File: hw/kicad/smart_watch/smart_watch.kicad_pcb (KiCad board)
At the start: 2 copper layers, 45 parts, among them J1 BATTERTY, J2 1051330001, J3 GC9A01, J4 JST_PH6, SW1 SW_Push, SW2 SW_Push, SW4 SW_Push, U1 STM32L476RGTx, U2 nPM1300-QEAA, U3 SHT41, U4 LIS2MDL, U5 CH340E

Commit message: start pcb
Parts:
- added R4: 10k, Resistor_SMD:R_0603_1608Metric, F.Cu at (92.7, 88.5)
- added SW3: SW_Push, smart_watch:TL6340, F.Cu at (110.5, 89.5)
- SW1, SW2, SW4: footprint Button_Switch_SMD:SW_SPST_TL3305A -> smart_watch:TL6340
- moved C50 110.0 mm to (214.7, 150.0)
- moved C51 110.0 mm to (214.7, 152.5)
- moved U3 97.2 mm to (187.8, 47.1)
- moved C30 89.0 mm to (189.5, 49.0)
- moved U2 87.0 mm to (62.0, 98.0)
- moved D1 81.2 mm to (202.6, 141.2)
- moved R30 79.1 mm to (185.5, 45.0), turned to -90 degrees
- moved R31 78.1 mm to (185.5, 49.0), turned to 90 degrees
- moved L20 76.2 mm to (46.5, 89.7), turned to -90 degrees
- moved L21 73.0 mm to (49.5, 99.3), turned to -90 degrees
- moved C25 70.7 mm to (48.0, 89.7), turned to -90 degrees
- moved C26 70.5 mm to (48.0, 99.3), turned to -90 degrees
- moved C27 64.0 mm to (55.0, 108.3), turned to -90 degrees
- moved R20 59.9 mm to (68.5, 107.7), turned to 90 degrees
- moved R21 57.8 mm to (70.0, 107.7), turned to 90 degrees
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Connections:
- SW1 pad 2: /BTN_2 -> /BTN_1
- SW2 pad 2: /BTN_3 -> /BTN_2
- SW4 pad 2: /BTN_1 -> /BTN_4
- U1 pad 10: /BTN_3 -> unconnected-(U1-PC2-Pad10)
- U1 pad 26: unconnected-(U1-PB0-Pad26) -> /BTN_2
- U1 pad 40: unconnected-(U1-PC9-Pad40) -> /BTN_3
- U1 pad 53: unconnected-(U1-PC12-Pad53) -> /BTN_4
- U1 pad 9: /BTN_2 -> unconnected-(U1-PC1-Pad9)
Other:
- rule pad_to_mask_clearance: 0 -> 0.0508

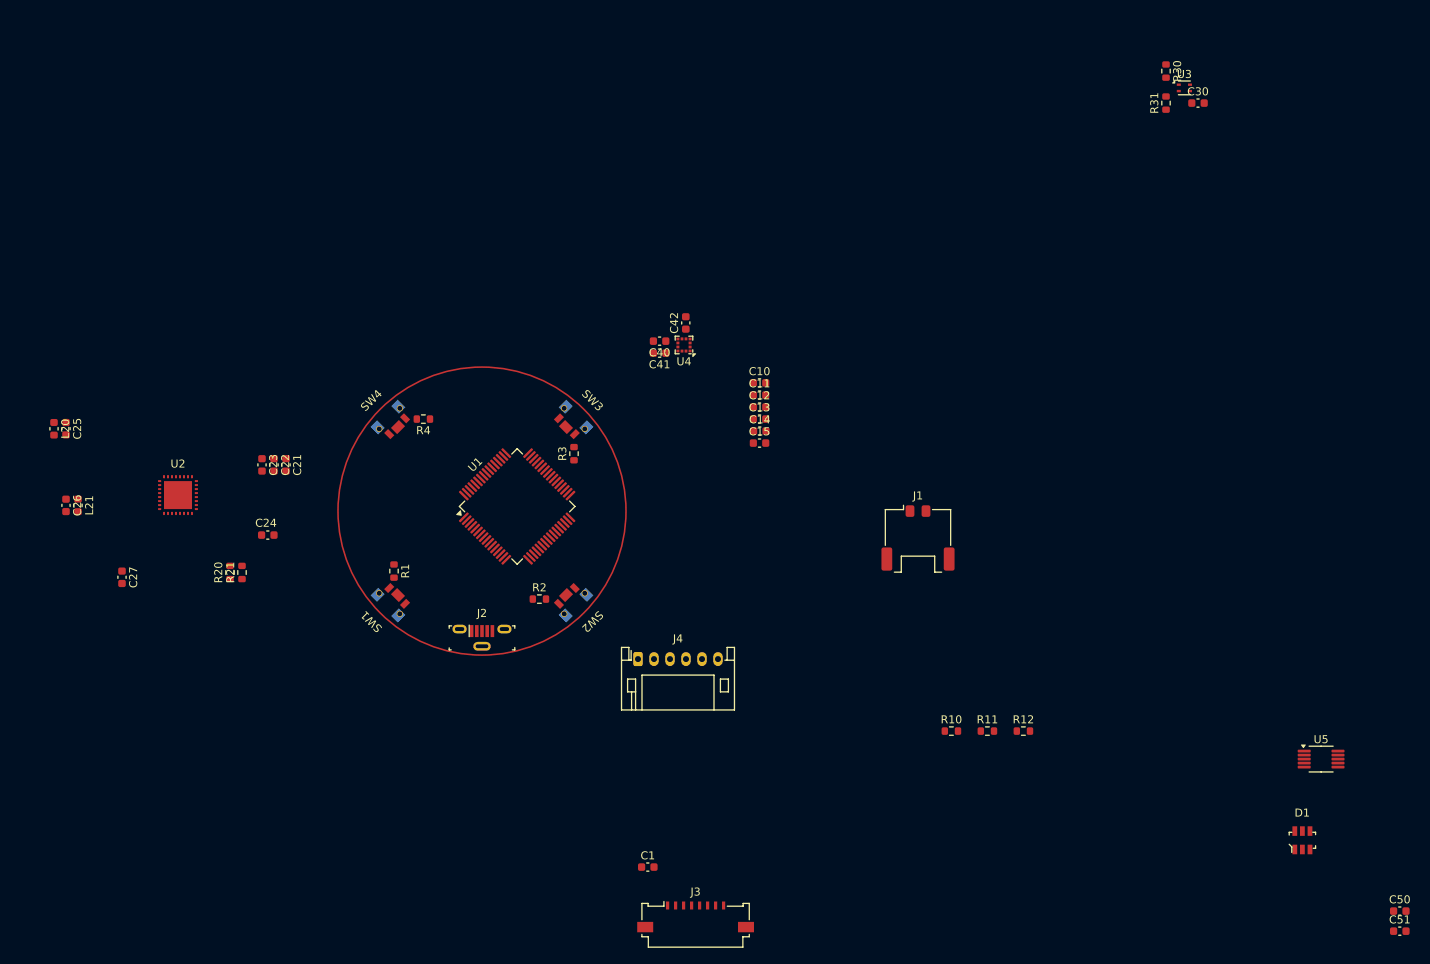
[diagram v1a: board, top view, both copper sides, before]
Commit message: added rtc chip to board
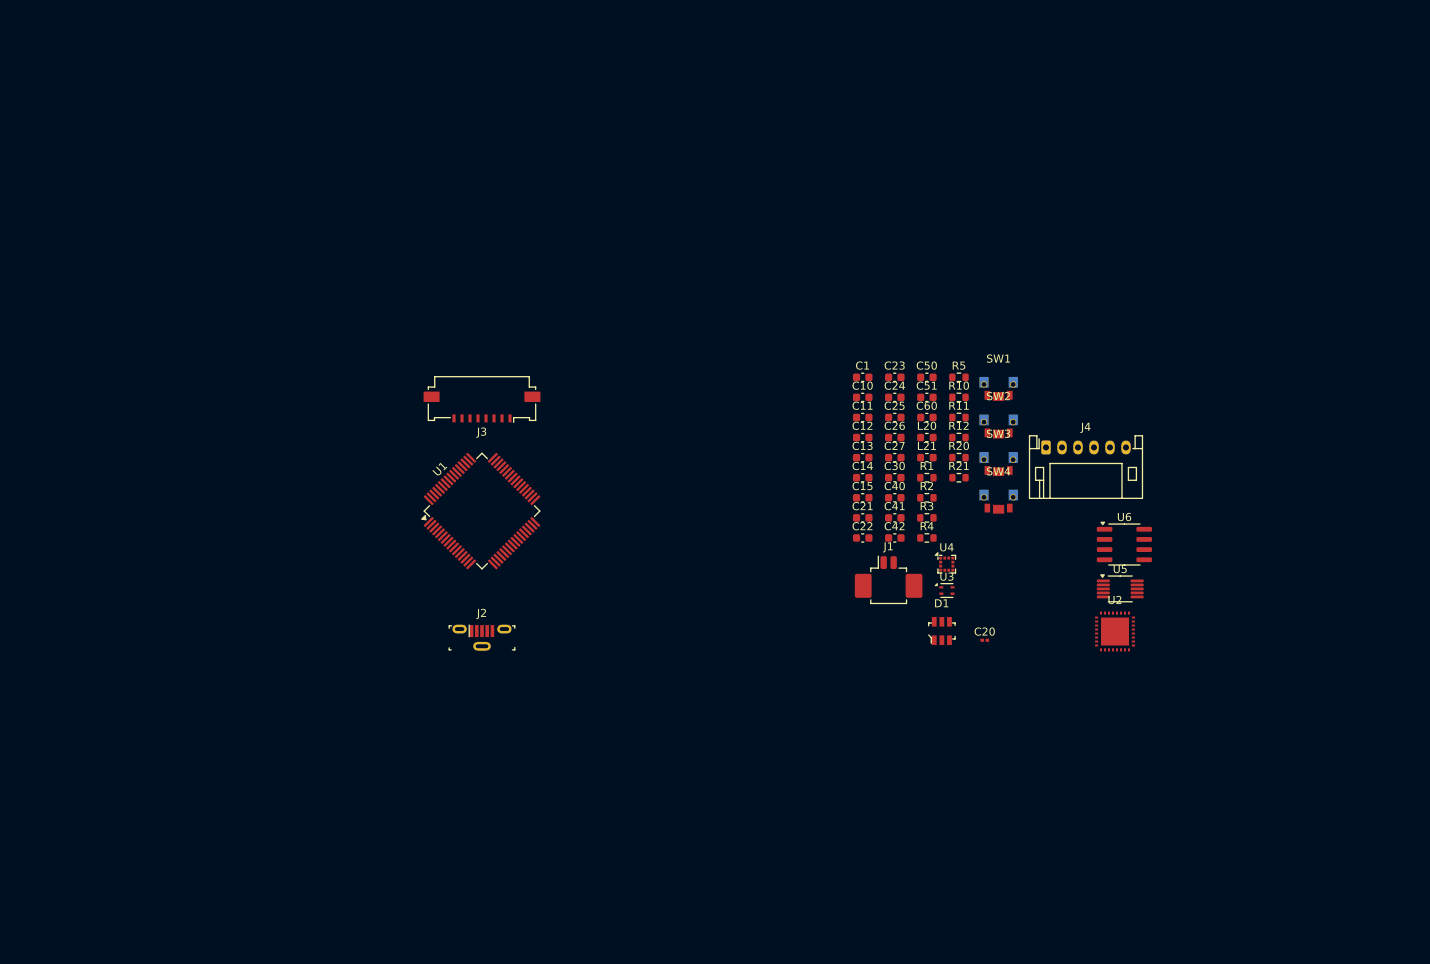
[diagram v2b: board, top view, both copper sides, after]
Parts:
- removed R30, R31: 10k, Resistor_SMD:R_0603_1608Metric
- added C20: 1u, Capacitor_SMD:C_0201_0603Metric, F.Cu at (162.8, 116.2)
- added C60: 100n, Capacitor_SMD:C_0603_1608Metric, F.Cu at (155.6, 88.3)
- added R5: 2.2k, Resistor_SMD:R_0603_1608Metric, F.Cu at (159.6, 83.3)
- added U6: DS3231MZ, Package_SO:SOIC-8_3.9x4.9mm_P1.27mm, F.Cu at (180.3, 104.2)
- C24, L21: value 220n -> 2.2u
- J1: footprint Connector_Molex:Molex_Pico-Lock_205338-0002_1x02-1MP_P2.00mm_Horizontal -> Connector_Molex:Molex_PicoBlade_53261-0271_1x02-1MP_P1.25mm_Horizontal
- L20: value 200n -> 2.2u
- moved U2 118.4 mm to (179.1, 115.1)
- moved L20 109.1 mm to (155.6, 90.8), turned to 0 degrees
- moved L21 106.3 mm to (155.6, 93.3), turned to 0 degrees
- moved C26 103.9 mm to (151.6, 90.8), turned to 0 degrees
- moved C25 103.6 mm to (151.6, 88.3), turned to 0 degrees
- moved C27 97.8 mm to (151.6, 93.3), turned to 0 degrees
- moved R20 92.2 mm to (159.6, 93.3), turned to 0 degrees
- moved R21 90.4 mm to (159.6, 95.8), turned to 0 degrees
- moved C50 89.1 mm to (155.6, 83.3)
- moved C51 89.1 mm to (155.6, 85.8)
- moved C24 80.2 mm to (151.6, 85.8)
- moved C23 79.9 mm to (151.6, 83.3), turned to 0 degrees
- moved SW1 79.1 mm to (164.6, 85.7), turned to 0 degrees
- moved SW4 75.8 mm to (164.6, 99.8), turned to 0 degrees
- moved C22 74.2 mm to (147.6, 103.4), turned to 0 degrees
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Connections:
- R11 pad 1: GND -> +3.3V
- R12 pad 2: GND -> +3.3V
- U1 pad 52: unconnected-(U1-PC11-Pad52) -> /RTC_INT

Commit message: pcb design part 1
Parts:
- C20: footprint Capacitor_SMD:C_0201_0603Metric -> Capacitor_SMD:C_0603_1608Metric
- J3: footprint Connector_FFC-FPC:Molex_200528-0080_1x08-1MP_P1.00mm_Horizontal -> Connector_FFC-FPC:Hirose_FH12-15S-0.5SH_1x15-1MP_P0.50mm_Horizontal; moved to B.Cu
- J4: value JST_PH6 -> JST_ZH6; footprint Connector_JST:JST_PH_S6B-PH-K_1x06_P2.00mm_Horizontal -> Connector_JST:JST_ZH_S6B-ZR-SM4A-TF_1x06-1MP_P1.50mm_Horizontal; moved to B.Cu
- moved U2 85.6 mm to (95.2, 98.0), turned to 180 degrees
- moved U6 82.6 mm to (100.0, 84.9), turned to 180 degrees
- moved SW1 80.3 mm to (88.5, 111.5), turned to 135 degrees
- moved SW4 76.9 mm to (88.5, 88.5), turned to 45 degrees
- moved U5 76.3 mm to (103.5, 111.2), turned to 90 degrees
- moved C20 72.9 mm to (91.8, 100.0), turned to -90 degrees
- moved R1 68.4 mm to (88.5, 108.9), turned to -90 degrees
- moved R20 66.4 mm to (93.2, 93.7), turned to -90 degrees
- moved R4 66.2 mm to (91.2, 88.2), turned to 180 degrees
- moved J1 66.1 mm to (85.3, 100.0), turned to -90 degrees
- moved R21 64.9 mm to (94.8, 93.7), turned to -90 degrees
- moved U4 63.1 mm to (97.5, 89.2)
- moved C24 60.6 mm to (91.8, 95.5), turned to 90 degrees
- moved C23 60.4 mm to (94.2, 102.3), turned to 90 degrees
- moved R11 59.8 mm to (101.0, 100.2), turned to -90 degrees
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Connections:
- D1 pad 4: Net-(U5-UD-) -> Net-(U5-UD+)
- D1 pad 6: Net-(U5-UD+) -> Net-(U5-UD-)
- J2 pad 2: Net-(D1-Pad3) -> Net-(D1-Pad1)
- J2 pad 3: Net-(D1-Pad1) -> Net-(D1-Pad3)
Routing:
- net +3.3V: track 0.00 -> 14.8 mm
- net +1.8V: track 0.00 -> 8.07 mm
- net Net-(J1-Pin_1): track 0.00 -> 7.80 mm
- net /VSYS: track 0.00 -> 4.24 mm
- net /I2C_SCL: track 0.00 -> 3.65 mm
- net Net-(U5-UD+): track 0.00 -> 2.89 mm
- net /I2C_SDA: track 0.00 -> 2.39 mm
- net Net-(U1-BOOT0): track 0.00 -> 2.32 mm
- net Net-(D1-Pad3): track 0.00 -> 2.31 mm
- net Net-(D1-Pad1): track 0.00 -> 2.21 mm
- net /RTC_INT: track 0.00 -> 1.94 mm
- net Net-(U2-VSET2): track 0.00 -> 1.91 mm
- net Net-(U2-VSET1): track 0.00 -> 1.89 mm
- net /VBUS: track 0.00 -> 1.59 mm
- net Net-(U4-C1): track 0.00 -> 1.25 mm
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
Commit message: pcb design part 2
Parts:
- added C16: 100n, Capacitor_SMD:C_0603_1608Metric, F.Cu at (101.9, 104.8)
- J4: moved to F.Cu
- moved J4 56.5 mm to (100.0, 87.6), turned to 180 degrees
- moved U4 22.2 mm to (106.6, 109.5)
- moved C42 22.1 mm to (106.1, 112.3)
- moved C40 22.1 mm to (109.4, 110.2)
- moved C41 22.1 mm to (109.4, 108.7)
- moved C15 20.8 mm to (105.1, 106.5), turned to 0 degrees
- moved J3 15.2 mm to (131.7, 85.5), turned to 0 degrees
- moved C12 14.6 mm to (115.4, 95.3)
- moved C30 14.6 mm to (91.9, 97.5)
- moved U3 14.5 mm to (94.7, 97.8)
- moved C60 10.7 mm to (98.8, 95.7)
- moved U6 10.7 mm to (94.3, 94.0)
- moved R5 10.6 mm to (98.8, 92.7), turned to 90 degrees
- moved C22 8.13 mm to (89.3, 105.7)
- moved C20 8.05 mm to (90.3, 108.0)
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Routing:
- net GND: track 0.00 -> 55.2 mm, vias 0 -> 28
- net /I2C_SDA: track 2.39 -> 37.2 mm, vias 0 -> 4
- net /BTN_1: track 0.00 -> 33.9 mm, vias 0 -> 2
- net +3.3V: track 14.8 -> 45.8 mm, vias 0 -> 13
- net /I2C_SCL: track 3.65 -> 33.3 mm, vias 0 -> 4
- net +1.8V: track 8.07 -> 33.5 mm, vias 0 -> 4
- net /BTN_2: track 0.00 -> 20.8 mm, vias 0 -> 2
- net /VBUS: track 1.59 -> 19.4 mm
- net /BTN_4: track 0.00 -> 17.2 mm, vias 0 -> 2
- net /VSYS: track 4.24 -> 19.4 mm, vias 0 -> 3
- net /RTC_INT: track 1.94 -> 11.4 mm, vias 0 -> 2
- net Net-(U2-SW2): track 0.00 -> 8.58 mm, vias 0 -> 2
- net Net-(U5-UD-): track 0.00 -> 7.40 mm
- net /BTN_3: track 0.00 -> 6.59 mm
- net /NRST: track 0.00 -> 3.11 mm, vias 0 -> 2
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- added copper zone on In2.Cu, net +3.3V
- added copper zone on In1.Cu, net GND
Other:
- board outline added: 37 x 37 mm
- copper layers 2 -> 4

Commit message: layout attempt 2
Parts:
- removed C1: 100n, Capacitor_SMD:C_0603_1608Metric
- removed C51: 100u, Capacitor_SMD:C_0603_1608Metric
- removed R1: 10k, Resistor_SMD:R_0603_1608Metric
- added C2: 0.1u, Capacitor_SMD:C_0603_1608Metric, F.Cu at (146.2, 62.0)
- J3: value GC9A01 -> GC9A01 / ER-TFT1.28-3; footprint Connector_FFC-FPC:Hirose_FH12-15S-0.5SH_1x15-1MP_P0.50mm_Horizontal -> smart_watch:GC9A01_FPC_pads_P0.5mm; moved to F.Cu
- J4: value JST_ZH6 -> ZH7; footprint Connector_JST:JST_ZH_S6B-ZR-SM4A-TF_1x06-1MP_P1.50mm_Horizontal -> Connector_JST:JST_ZH_S7B-ZR-SM4A-TF_1x07-1MP_P1.50mm_Horizontal
- moved D1 87.9 mm to (178.7, 73.5)
- moved C50 82.4 mm to (178.9, 79.1), turned to 0 degrees
- moved J2 80.0 mm to (171.6, 79.8)
- moved R10 78.0 mm to (151.5, 40.6), turned to 0 degrees
- moved U5 77.4 mm to (171.6, 74.5), turned to 0 degrees
- moved R11 76.7 mm to (151.5, 43.1), turned to 0 degrees
- moved R12 76.7 mm to (151.5, 45.6), turned to 0 degrees
- moved C10 69.1 mm to (147.5, 42.8), turned to 0 degrees
- moved C15 66.4 mm to (147.5, 55.4)
- moved C14 65.6 mm to (147.5, 52.9), turned to 0 degrees
- moved C16 65.4 mm to (147.5, 57.9), turned to 0 degrees
- moved C11 65.4 mm to (147.5, 45.4), turned to 0 degrees
- moved C13 60.8 mm to (147.5, 50.4), turned to 0 degrees
- moved C12 57.3 mm to (147.5, 47.9), turned to 0 degrees
- moved C23 56.8 mm to (103.7, 54.5), turned to 0 degrees
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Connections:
- J3 pad 1: +3.3V -> GND
- J3 pad 10: (no net) -> unconnected-(J3-Pin_10-Pad10)
- J3 pad 11: (no net) -> GND
- J3 pad 12: (no net) -> unconnected-(J3-Pin_12-Pad12)
- J3 pad 13: (no net) -> unconnected-(J3-Pin_13-Pad13)
- J3 pad 14: (no net) -> unconnected-(J3-Pin_14-Pad14)
- J3 pad 15: (no net) -> unconnected-(J3-Pin_15-Pad15)
- J3 pad 2: GND -> unconnected-(J3-Pin_2-Pad2)
- J3 pad 3: /SPI_MOSI -> unconnected-(J3-Pin_3-Pad3)
- J3 pad 4: /SPI_SCLK -> +3.3V
- J3 pad 5: /SPI_CS -> /SPI_DC
- J3 pad 6: /SPI_DC -> /SPI_CS
- J3 pad 7: /SPI_RST -> /SPI_SCLK
- J3 pad 8: +3.3V -> /SPI_MOSI
- J3 pad 9: (no net) -> /SPI_RST
- J4 pad 3: /SWCLK -> /NRST
- J4 pad 4: /SWDIO -> /SWO
- J4 pad 5: /NRST -> /TDI
- J4 pad 6: unconnected-(J4-Pin_6-Pad6) -> /SWCLK
- SW1 pad 1: +3.3V -> /NRST
- SW1 pad 2: /BTN_1 -> GND
- U1 pad 26: /BTN_2 -> unconnected-(U1-PB0-Pad26)
- U1 pad 50: unconnected-(U1-PA15-Pad50) -> /TDI
- U1 pad 55: unconnected-(U1-PB3-Pad55) -> /SWO
- U1 pad 8: /BTN_1 -> /BTN_2
- U5 pad 4: Net-(U5-~{RTS}) -> unconnected-(U5-~{RTS}-Pad4)
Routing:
- net GND: track 55.2 -> 0.00 mm, vias 28 -> 0
- net +3.3V: track 45.8 -> 0.00 mm, vias 13 -> 0
- net /I2C_SDA: track 37.2 -> 0.00 mm, vias 4 -> 0
- net /BTN_1: track 33.9 -> 0.00 mm, vias 2 -> 0
- net +1.8V: track 33.5 -> 0.00 mm, vias 4 -> 0
- net /I2C_SCL: track 33.3 -> 0.00 mm, vias 4 -> 0
- net /BTN_2: track 20.8 -> 0.00 mm, vias 2 -> 0
- net /VBUS: track 19.4 -> 0.00 mm
- net /VSYS: track 19.4 -> 0.00 mm, vias 3 -> 0
- net /BTN_4: track 17.2 -> 0.00 mm, vias 2 -> 0
- net /RTC_INT: track 11.4 -> 0.00 mm, vias 2 -> 0
- net Net-(U2-SW2): track 8.58 -> 0.00 mm, vias 2 -> 0
- net Net-(J1-Pin_1): track 7.83 -> 0.00 mm
- net Net-(U5-UD-): track 7.40 -> 0.00 mm
- net /BTN_3: track 6.59 -> 0.00 mm
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- removed copper zone on In2.Cu, net +3.3V
- removed copper zone on In1.Cu, net GND
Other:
- copper layers 4 -> 2
- rule pad_to_mask_clearance: 0.0508 -> 0

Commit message: layout attempt 2 part 2
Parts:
- J4: moved to B.Cu
- moved C13 79.9 mm to (90.7, 106.6), turned to 180 degrees
- moved C14 77.2 mm to (90.0, 104.3), turned to -90 degrees
- moved R12 76.4 mm to (91.9, 93.5), turned to 180 degrees
- moved R10 75.5 mm to (97.9, 93.7)
- moved R11 75.0 mm to (95.2, 92.6), turned to -90 degrees
- moved C12 74.5 mm to (103.5, 108.0)
- moved C50 74.2 mm to (107.9, 100.8)
- moved C15 71.9 mm to (90.0, 98.6), turned to -90 degrees
- moved D1 70.8 mm to (111.8, 96.8)
- moved C10 68.2 mm to (103.9, 95.3), turned to 90 degrees
- moved U5 67.4 mm to (108.0, 96.7), turned to -90 degrees
- moved C16 66.9 mm to (91.9, 95.1), turned to 180 degrees
- moved C11 65.4 mm to (105.4, 95.3), turned to 90 degrees
- moved C2 60.8 mm to (92.2, 89.9), turned to 180 degrees
- moved J2 60.1 mm to (115.0, 100.0), turned to 90 degrees
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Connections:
- J4 pad 1: +3.3V -> /SWDIO
- J4 pad 2: GND -> /SWCLK
- J4 pad 3: /NRST -> /TDI
- J4 pad 5: /TDI -> /NRST
- J4 pad 6: /SWCLK -> GND
- J4 pad 7: /SWDIO -> +3.3V
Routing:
- net /I2C_SDA: track 0.00 -> 51.8 mm, vias 0 -> 6
- net /I2C_SCL: track 0.00 -> 50.6 mm, vias 0 -> 5
- net +3.3V: track 0.00 -> 35.7 mm, vias 0 -> 1
- net /NRST: track 0.00 -> 30.6 mm, vias 0 -> 3
- net /VSYS: track 0.00 -> 26.5 mm, vias 0 -> 3
- net +1.8V: track 0.00 -> 26.2 mm, vias 0 -> 2
- net /VBUS: track 0.00 -> 23.7 mm, vias 0 -> 3
- net /RTC_INT: track 0.00 -> 23.6 mm, vias 0 -> 2
- net /USART_TX: track 0.00 -> 22.5 mm, vias 0 -> 2
- net Net-(J1-Pin_1): track 0.00 -> 22.5 mm, vias 0 -> 2
- net /BTN_4: track 0.00 -> 22.4 mm, vias 0 -> 2
- net /USART_RX: track 0.00 -> 19.9 mm, vias 0 -> 2
- net /SPI_DC: track 0.00 -> 18.6 mm, vias 0 -> 2
- net GND: track 0.00 -> 18.6 mm, vias 0 -> 1
- net /SPI_CS: track 0.00 -> 18.5 mm, vias 0 -> 2
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- added copper zone on In2.Cu, net +3.3V
- added copper zone on In1.Cu, net GND
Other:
- copper layers 2 -> 4

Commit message: layout attempt 2 part 3
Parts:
- moved C50 1.40 mm to (109.3, 100.8)
- moved R21 0.10 mm to (102.3, 92.7)
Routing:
- net GND: track 18.6 -> 88.9 mm, vias 1 -> 30
- net +3.3V: track 35.7 -> 64.6 mm, vias 1 -> 14
- net +1.8V: track 26.2 -> 43.0 mm, vias 2 -> 4
- net /NRST: track 30.6 -> 45.4 mm, vias 3 -> 4
- net Net-(U4-C1): track 0.00 -> 1.46 mm
- net /I2C_SCL: track 50.6 -> 51.2 mm

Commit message: back at the pcb design
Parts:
- J1: moved to B.Cu
- moved R10 0.35 mm to (97.6, 93.7)
- turned J1 to 90 degrees
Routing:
- net GND: track 88.9 -> 86.4 mm, vias 30 -> 31
- net Net-(J1-Pin_1): track 22.5 -> 23.1 mm
- net Net-(U1-BOOT0): track 2.67 -> 2.17 mm
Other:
- board size 37 x 37 mm -> 36 x 36 mm
